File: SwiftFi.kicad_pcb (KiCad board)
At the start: 2 copper layers, 79.6 x 67.6 mm, 38 parts, among them J1 Addl Signals, J2 Programming, Q1 BSS138, Q2 BSS138, Q3 BSS138, Q4 BSS138, Q5 BSS138, U1 6526, U2 6551, U3 74HC74, U4 ESP-12E, U5 LM1117-3.3, Y1 3.6864 MHz

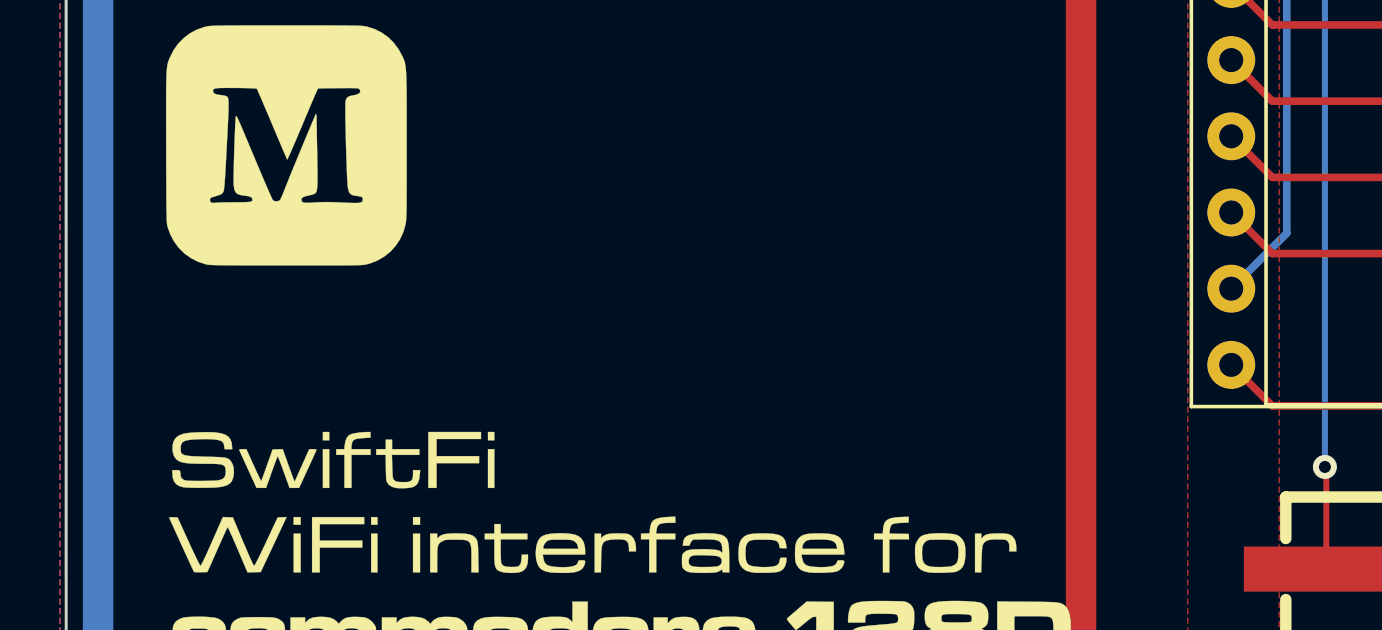
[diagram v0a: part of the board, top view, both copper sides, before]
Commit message: Added GitHub repo URL to PCB silkscreen
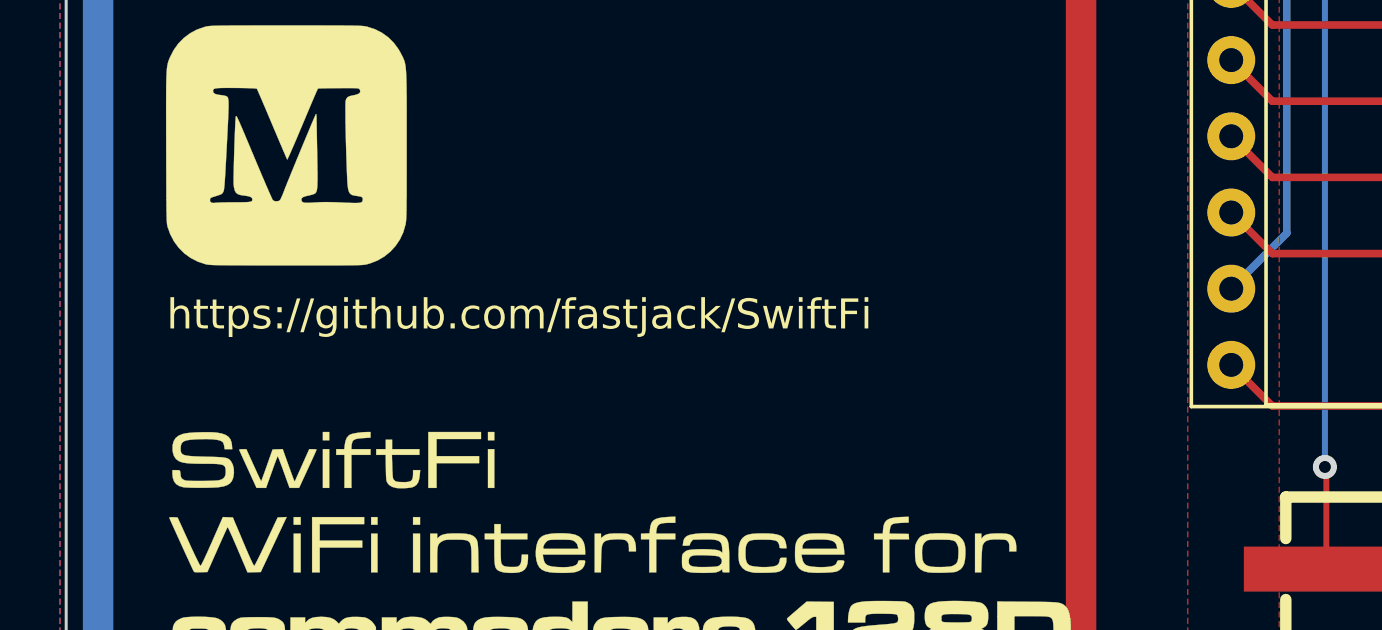
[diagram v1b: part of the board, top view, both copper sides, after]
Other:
- board text added: "https://github.com/fastjack/SwiftFi"
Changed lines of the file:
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@@
     (effects (font (size 1 1) (thickness 0.15)))
+  )
+  (gr_text "https://github.com/fastjack/SwiftFi" (at 117.602 108.458) (layer "F.SilkS")
+    (effects (font (size 1 1) (thickness 0.15)) (justify left))
   )
   (gr_text "ESP-12" (at 139.192 65.786) (layer "F.SilkS")

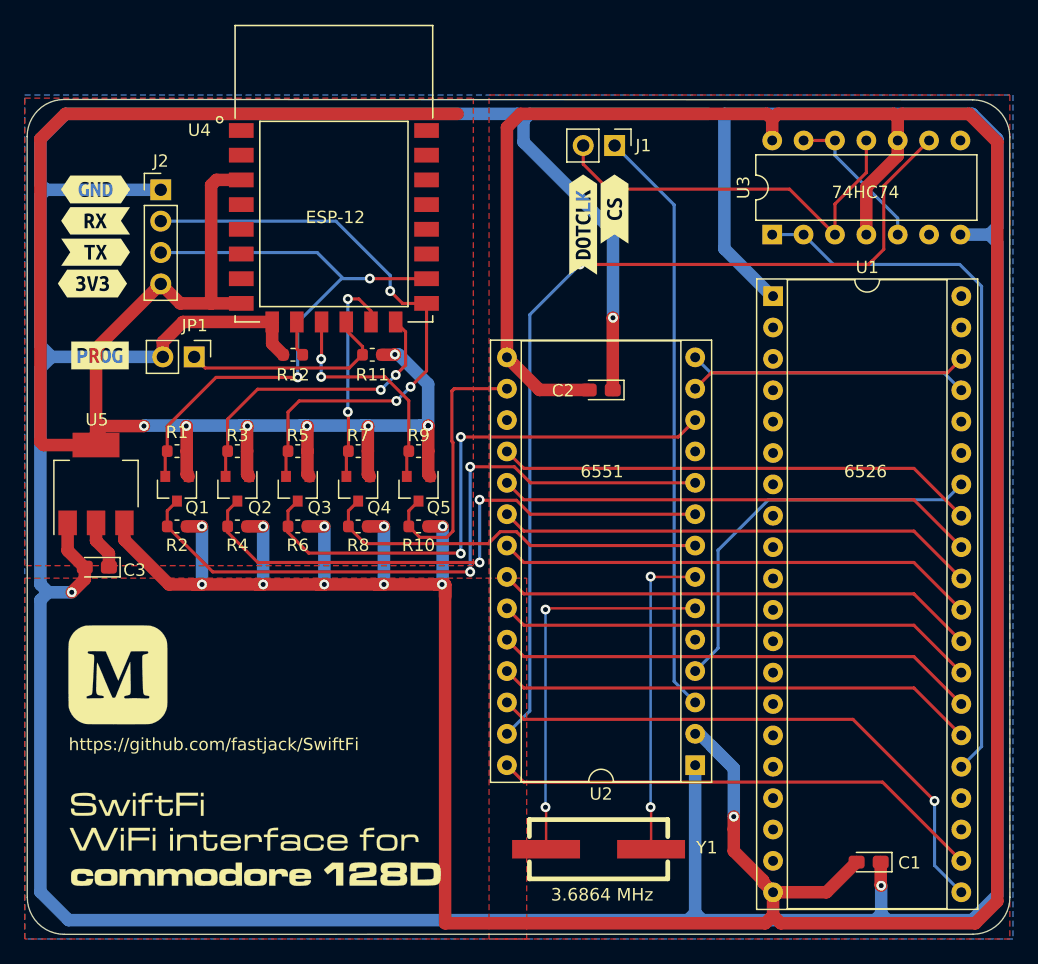
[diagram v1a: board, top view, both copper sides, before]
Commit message: changed footprints caps, added llinks to aliexpress in BOM
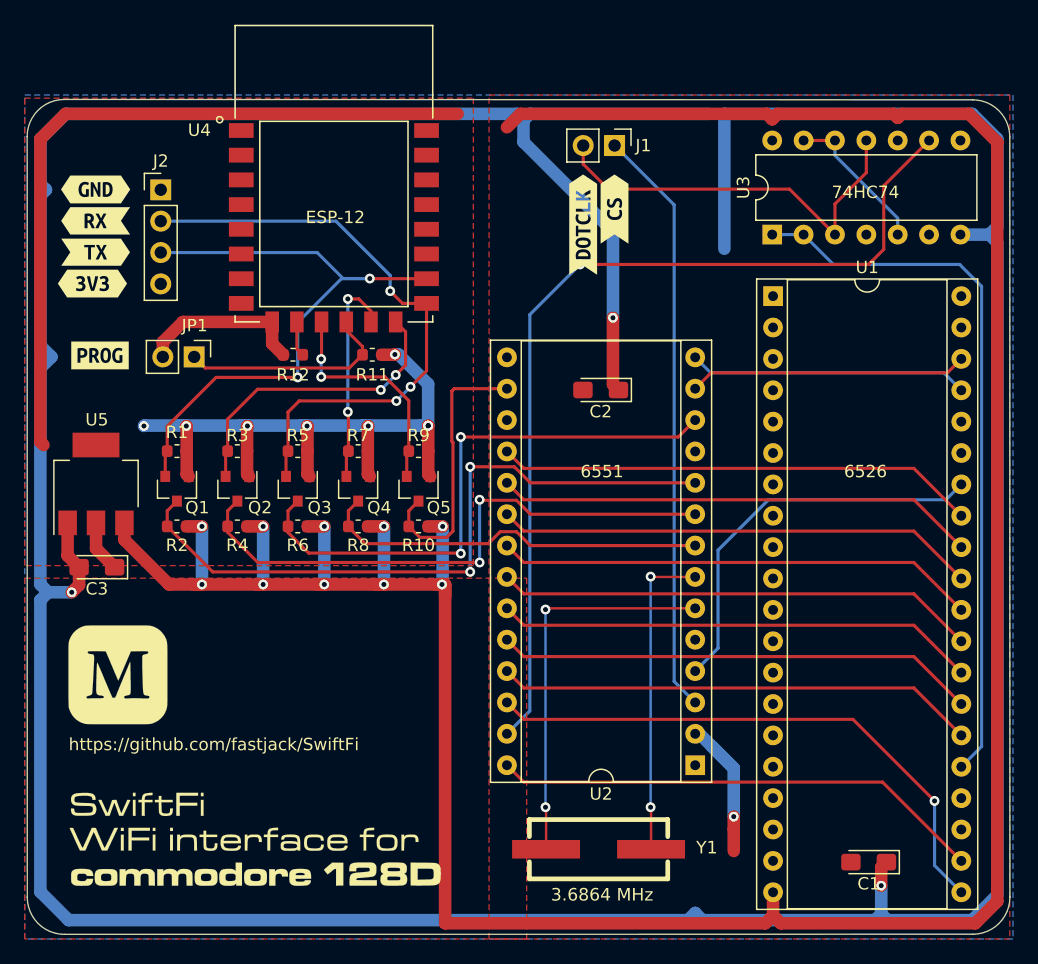
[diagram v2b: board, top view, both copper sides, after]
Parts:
- C1, C2, C3: footprint Capacitor_Tantalum_SMD:CP_EIA-2012-12_Kemet-R_Pad1.30x1.05mm_HandSolder -> Capacitor_Tantalum_SMD:CP_EIA-3216-10_Kemet-I_Pad1.58x1.35mm_HandSolder
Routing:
- net +5V: track 305.5 -> 254.5 mm
- net +3V3: track 161.5 -> 117.8 mm
- net GND: track 383.3 -> 347.5 mm

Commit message: enlarged drill holes for pins of CIA
the individual pins intended to be used here require drill holes of 1.5 mm in diameter
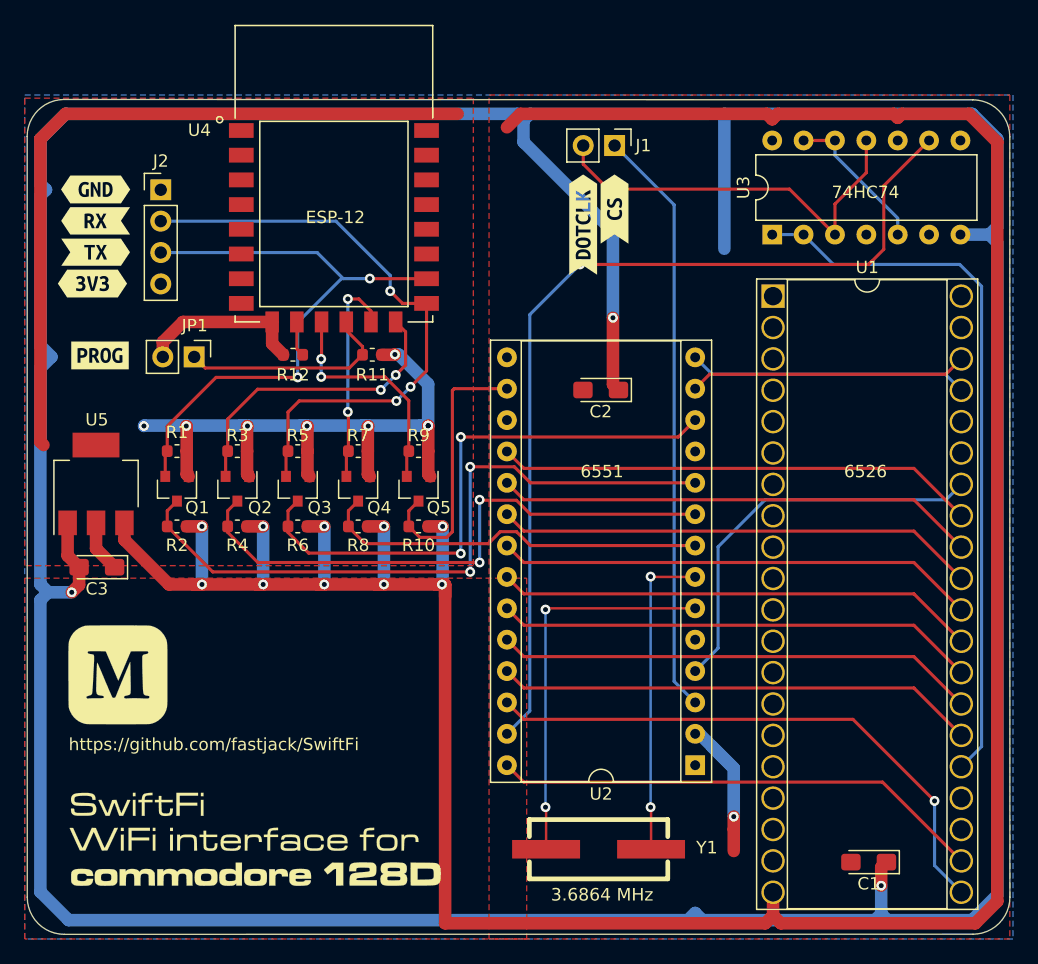
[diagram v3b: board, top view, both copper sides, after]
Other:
- rule pad_to_mask_clearance: 0 -> 0.0508

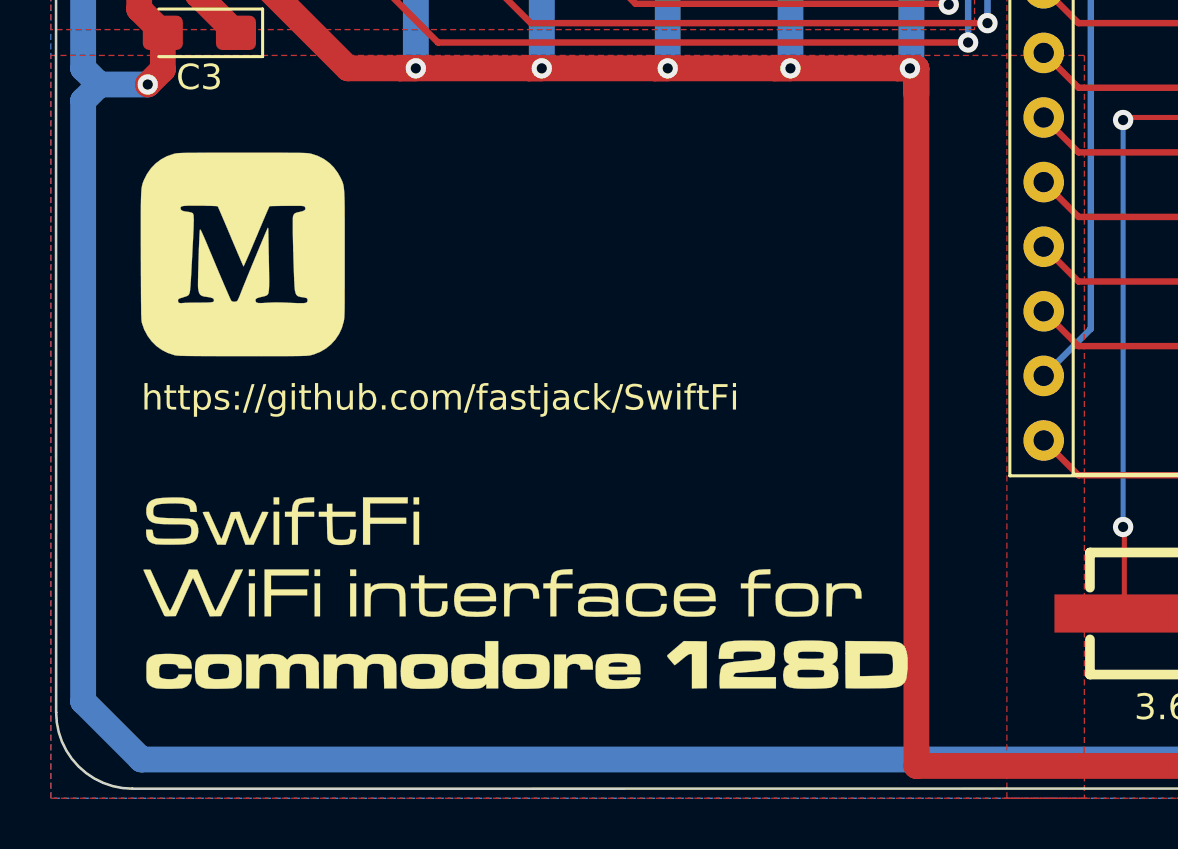
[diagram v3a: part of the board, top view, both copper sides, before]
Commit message: Updated logo
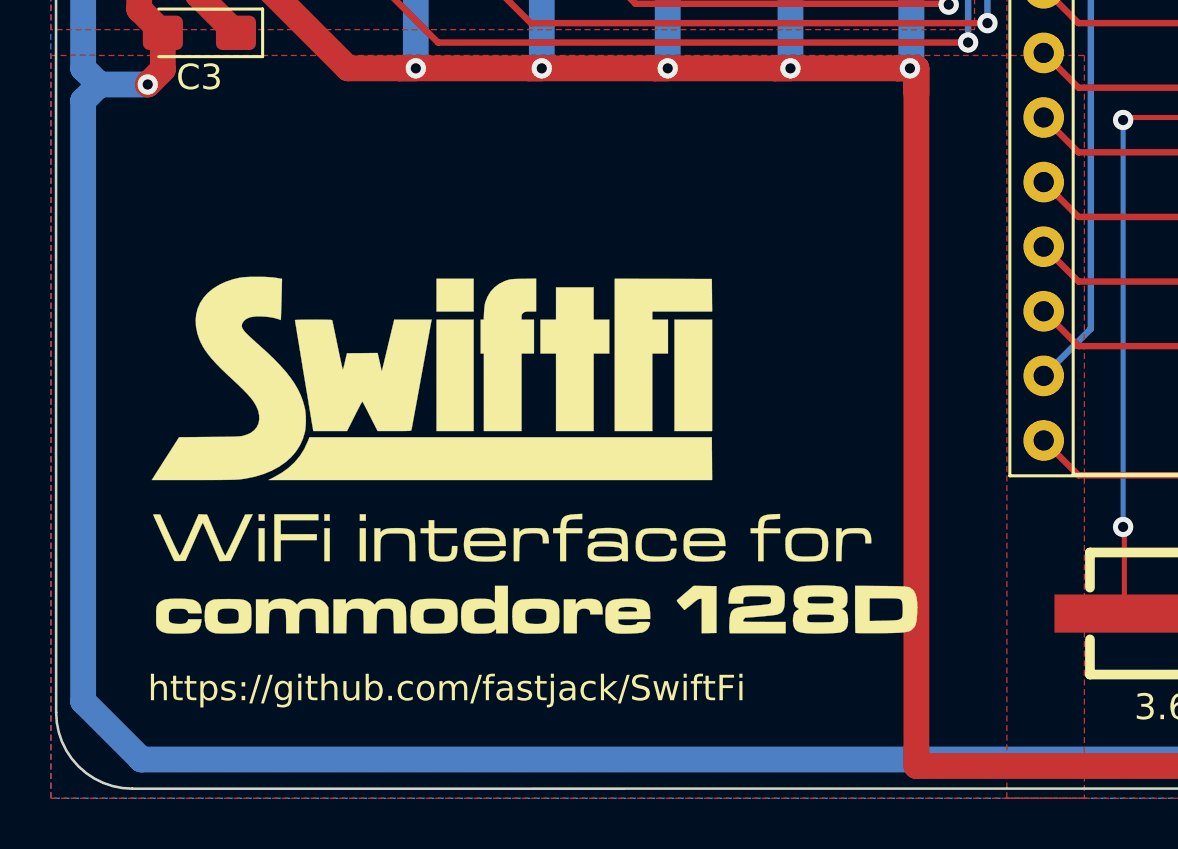
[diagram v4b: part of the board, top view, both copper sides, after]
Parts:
- removed the G*** at (133.1, 115.3)
- removed M_LOGO: LOGO, M-Logo-08:F.SilkS_g17
- added G***: LOGO, Martins Logos:WiFi interface Text, F.Cu at (133.5, 113.1)
- added G***: LOGO, Martins Logos:Logo 7mm, B.Cu at (120.9, 117.3)
- added Ref**: Val**, Martins Logos:SwiftFi 8mm, F.Cu at (133.2, 111.1)
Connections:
- net /R~W renamed /R~{W}
- net /~IRQ renamed /~{IRQ}
- net /~RESET renamed /~{RESET}
